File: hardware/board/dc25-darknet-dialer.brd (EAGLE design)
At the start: 101.6 x 101.6 mm, 81 parts, among them SW1 RESET, X1 USB-MICROB, Y1 RESONATORSMD

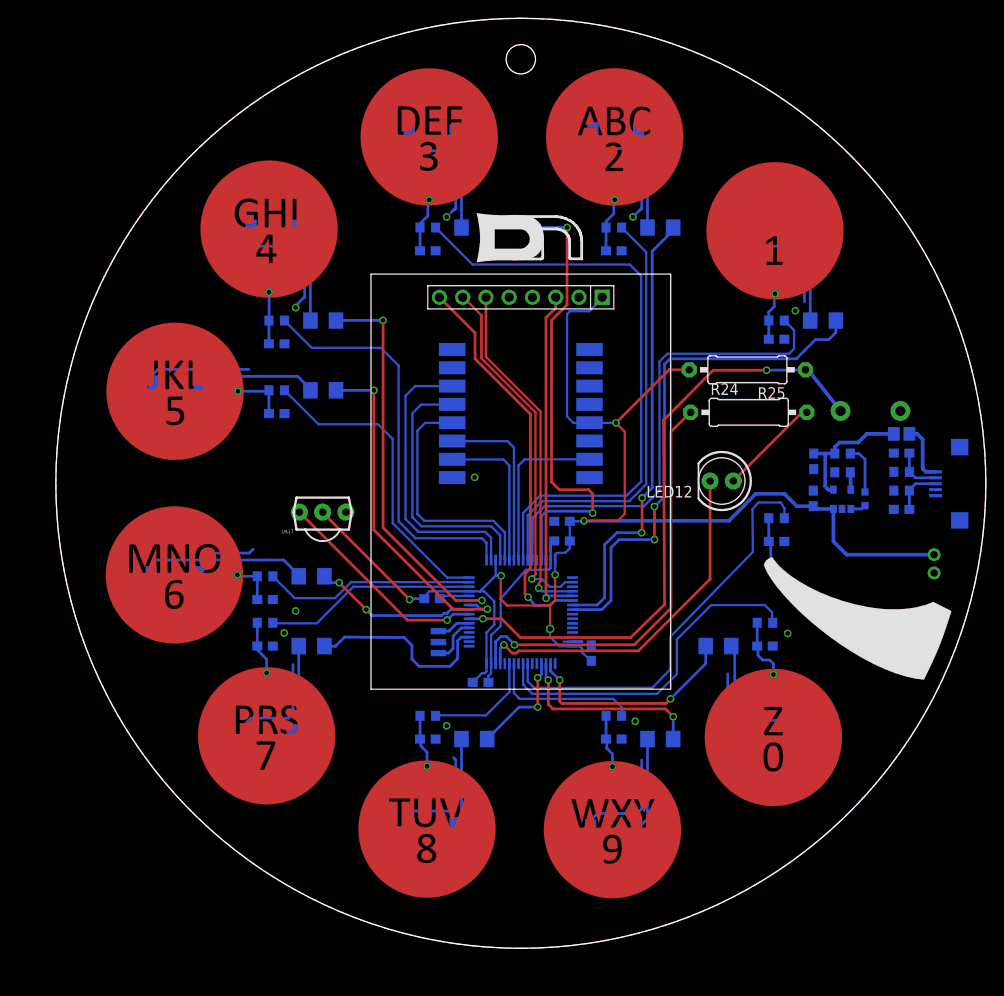
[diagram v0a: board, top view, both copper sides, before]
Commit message: Additional details on power, added fuse and prep for 3.3v LDO
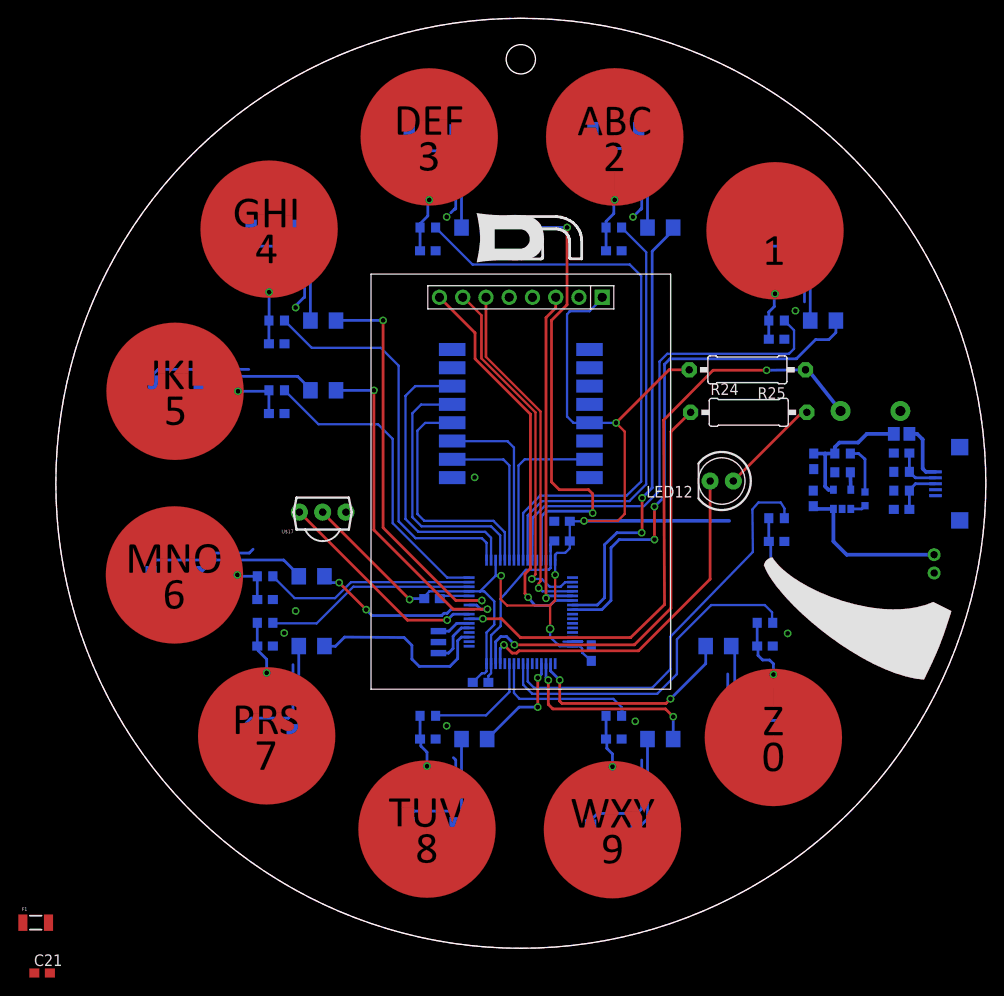
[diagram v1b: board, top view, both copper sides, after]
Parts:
- added C21: (no value), SYNShop:C0603
- added F1: 500uA, SparkFun:PTC-1206
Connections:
- new net N$31: F1.2
- new net VCC1: C17.2, CN1.2, F1.1, U$11.3
- net GND: now also C21.1
- net VCC: now also C21.2; no longer C17.2, CN1.2, U$11.3
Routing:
- net VCC: track 159.4 -> 130.9 mm
- net VCC1: track 0.00 -> 17.5 mm
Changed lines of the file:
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@@
 <element name="L1" library="dp_devices" package="FB603" value="" x="92.4" y="56.2" rot="MR180"/>
 <element name="Y1" library="SparkFun" package="RESONATOR-SMD" value="RESONATORSMD" x="41.8" y="33.45" rot="MR90"/>
+<element name="F1" library="SparkFun" package="PTC-1206" value="500uA" x="-2.2" y="2.8"/>
+<element name="C21" library="SYNShop" package="C0603" value="" x="-1.5" y="-2.7"/>
 </elements>
 <signals>
@@
 <via x="80.8" y="69.65" extent="1-16" drill="0.5"/>
 <contactref element="Y1" pad="2"/>
+<contactref element="C21" pad="1"/>
+<wire x1="20.828" y1="23.344" x2="-2.35" y2="-2.7" width="0" layer="19" extent="1-16"/>
 </signal>
 <signal name="N$1">
@@
 <wire x1="54" y1="34.9" x2="54" y2="37.45" width="0.254" layer="1"/>
 <wire x1="54" y1="37.45" x2="54.55" y2="38" width="0.254" layer="1"/>
-<contactref element="U$11" pad="3"/>
-<contactref element="C17" pad="2"/>
-<wire x1="84.95" y1="48" x2="83.15" y2="48" width="0.4064" layer="16"/>
-<wire x1="83.15" y1="48" x2="82.75" y2="48.3" width="0.4064" layer="16"/>
 <contactref element="U$17" pad="2"/>
-<contactref element="CN1" pad="2"/>
-<wire x1="95.95" y1="43" x2="86.4" y2="43" width="0.4064" layer="16"/>
-<wire x1="86.4" y1="43" x2="84.95" y2="44.45" width="0.4064" layer="16"/>
-<wire x1="84.95" y1="44.45" x2="84.95" y2="48" width="0.4064" layer="16"/>
 <contactref element="R25" pad="2"/>
-<wire x1="82.75" y1="48.3" x2="80.95" y2="48.3" width="0.4064" layer="16"/>
-<wire x1="80.95" y1="48.3" x2="79.6" y2="49.65" width="0.4064" layer="16"/>
-<wire x1="79.6" y1="49.65" x2="76.45" y2="49.65" width="0.4064" layer="16"/>
-<wire x1="76.45" y1="49.65" x2="73.55" y2="46.7" width="0.4064" layer="16"/>
 <wire x1="73.55" y1="46.7" x2="57.7" y2="46.7" width="0.4064" layer="16"/>
 <wire x1="69.2" y1="63.2" x2="67" y2="63.2" width="0.3048" layer="1"/>
@@
 <wire x1="38.75" y1="38.1" x2="38.85" y2="38.2" width="0.3048" layer="16"/>
 <wire x1="38.85" y1="38.2" x2="40.25" y2="38.2" width="0.3048" layer="16"/>
+<contactref element="C21" pad="2"/>
+<wire x1="-0.65" y1="-2.7" x2="45.55" y2="29.05" width="0" layer="19" extent="1-16"/>
 </signal>
 <signal name="TSC_G3_IO2">
@@
 <contactref element="U$2" pad="P30"/>
 </signal>
+<signal name="VCC1">
+<contactref element="U$11" pad="3"/>
+<contactref element="C17" pad="2"/>
+<contactref element="CN1" pad="2"/>
+<wire x1="84.95" y1="48" x2="83.15" y2="48" width="0.4064" layer="16"/>
+<wire x1="83.15" y1="48" x2="82.75" y2="48.3" width="0.4064" layer="16"/>
+<wire x1="95.95" y1="43" x2="86.4" y2="43" width="0.4064" layer="16"/>
+<wire x1="86.4" y1="43" x2="84.95" y2="44.45" width="0.4064" layer="16"/>
+<wire x1="84.95" y1="44.45" x2="84.95" y2="48" width="0.4064" layer="16"/>
+<contactref element="F1" pad="1"/>
+<wire x1="-3.6" y1="2.8" x2="82.75" y2="48.3" width="0" layer="19" extent="1-16"/>
+</signal>
+<signal name="N$31">
+<contactref element="F1" pad="2"/>
+</signal>
 </signals>
